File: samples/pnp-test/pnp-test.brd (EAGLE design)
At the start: 76.2 x 76.2 mm, 34 parts

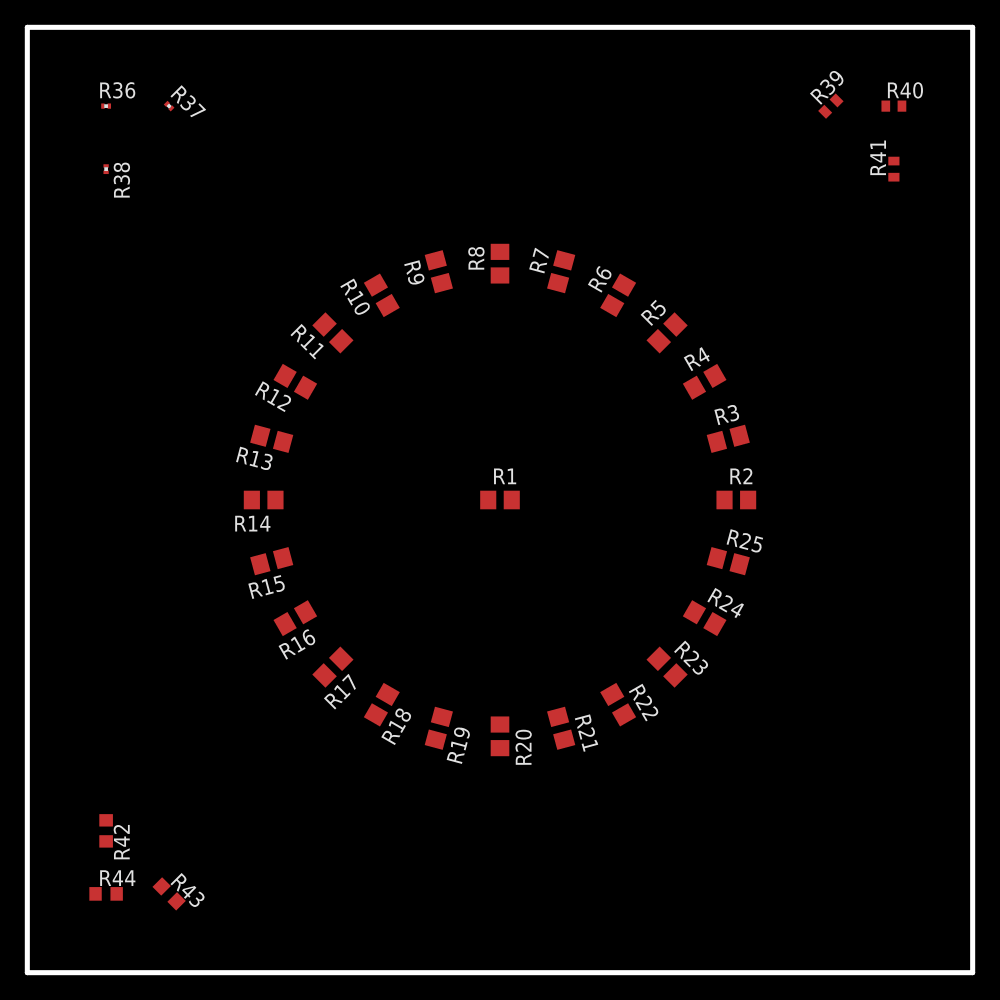
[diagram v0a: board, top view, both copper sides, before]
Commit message: Dumped a bunch of old samples that are no longer used. Updated and exported the pnp-test board so it can be used with image camera.
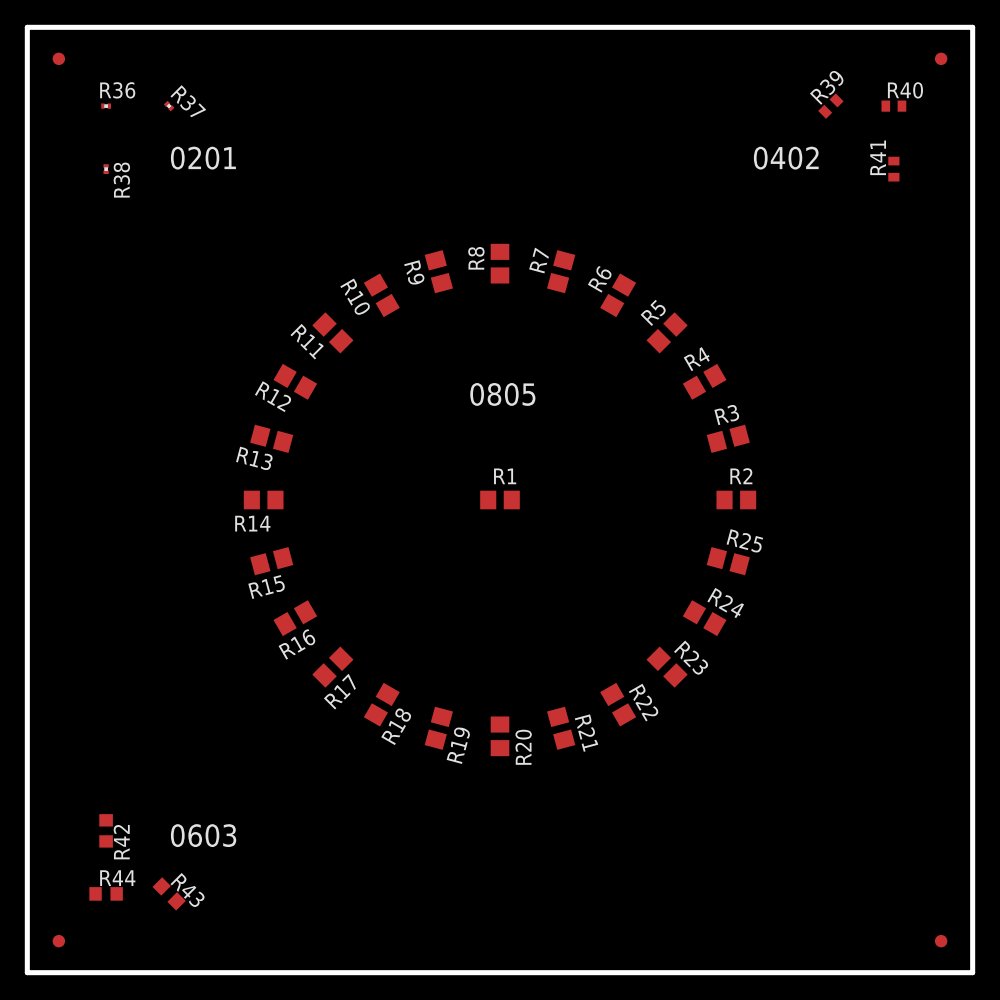
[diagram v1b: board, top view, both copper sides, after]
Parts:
- added U$1, U$2, U$3, U$4: FIDUCIAL1X2, SparkFun:FIDUCIAL-1X2
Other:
- board text added: "0201"
- board text added: "0402"
- board text added: "0603"
- board text added: "0805"

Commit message: Put together a full demo suite. Fresh install now boots clean and can immediately run the pnp-test job.
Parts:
- removed U$1, U$2, U$3, U$4: FIDUCIAL1X2, SparkFun:FIDUCIAL-1X2
- added FID1, FID2, FID3, FID4: FIDUCIAL1X2, SparkFun:FIDUCIAL-1X2
- R1, R10, R11, R12, R13, R14, R15, R16, R17, R18, R19, R2, R20, R21, R22, R23, R24, R25, R3, R36, R37, R38, R39, R4, R40, R41, R42, R43, R44, R5, R6, R7, R8, R9: value (none) -> 1K
- moved R17 5.09 mm to (21.0, 21.0)
- moved R16 5.09 mm to (17.2, 26.0)
- moved R18 5.09 mm to (26.0, 17.2)
- moved R15 5.07 mm to (14.8, 31.8)
- moved R19 5.07 mm to (31.8, 14.8)
- moved R14 5.05 mm to (14.0, 38.0)
- moved R20 5.05 mm to (38.0, 14.0)
- moved R13 5.02 mm to (14.8, 44.2)
- moved R21 5.02 mm to (44.2, 14.8)
- moved R12 4.99 mm to (17.2, 50.0)
- moved R22 4.99 mm to (50.0, 17.2)
- moved R11 4.95 mm to (21.0, 55.0)
- moved R23 4.95 mm to (55.0, 21.0)
- moved R10 4.92 mm to (26.0, 58.8)
- moved R24 4.92 mm to (58.8, 26.0)
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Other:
- board size 76.2 x 76.2 mm -> 76 x 76 mm
- board text added: "FID1"
- board text added: "FID2"
- board text added: "FID3"
- board text added: "FID4"
